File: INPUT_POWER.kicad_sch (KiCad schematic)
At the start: 30 parts, among them J1 TYPE-C-31-M12_13, SW3 ON/OFF, U3 IP5306

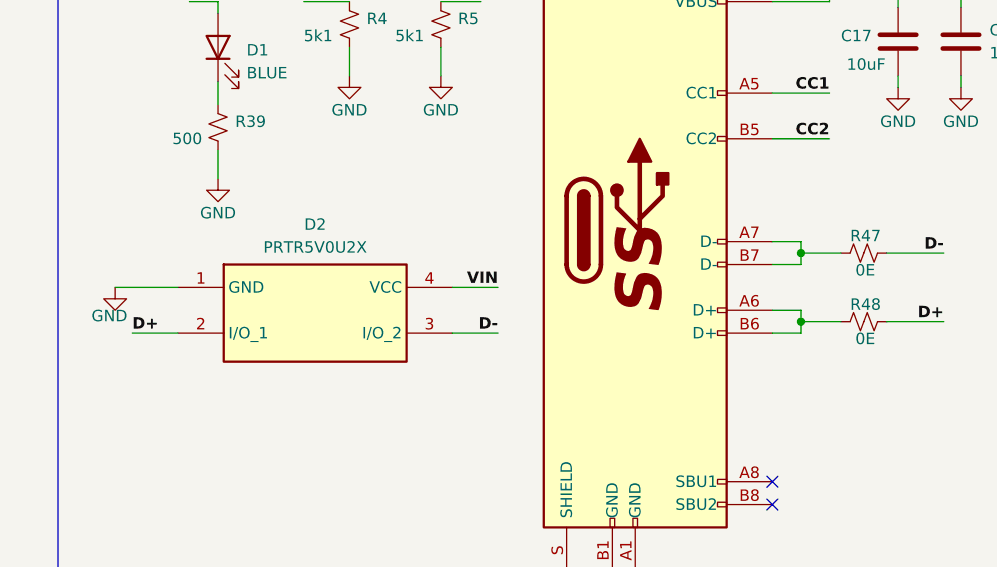
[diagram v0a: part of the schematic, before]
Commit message: Completed routing for USB peripheral for CH340
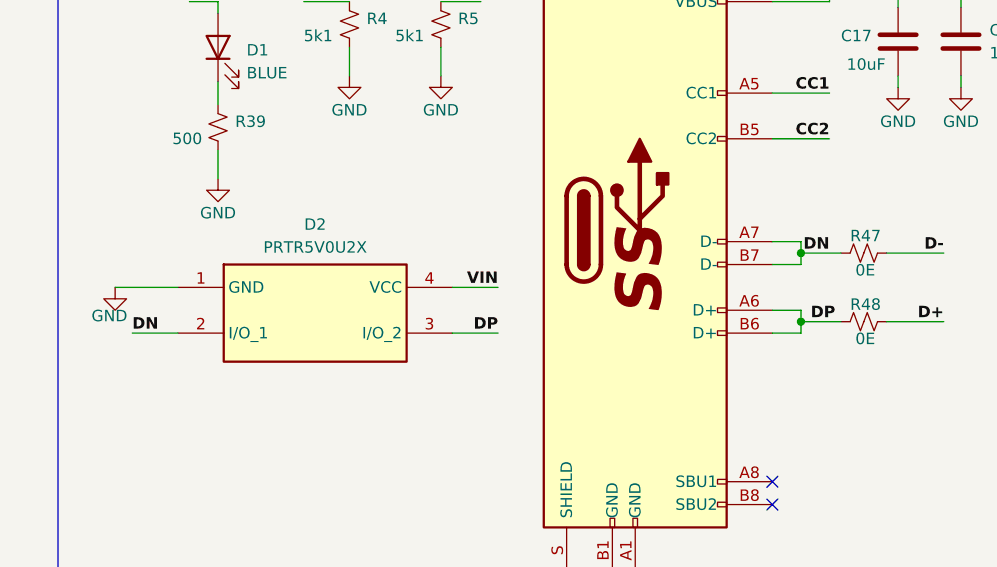
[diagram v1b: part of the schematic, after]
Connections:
- net D+: no longer D2.2 (I/O_1)
- net D-: no longer D2.3 (I/O_2)
- net DP: now reaches J1.A6 (D+), J1.B6 (D+), R48.1
- net DP: now also D2.3 (I/O_2)
- net DN: now reaches J1.A7 (D-), J1.B7 (D-), R47.1
- net DN: now also D2.2 (I/O_1)
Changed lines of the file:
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@@
     (effects (font (size 1.27 1.27) bold (color 0 255 0 1)) (justify left bottom))
   )
-  (label "D-" (at 69.215 95.25 180) (fields_autoplaced)
-    (effects (font (size 1.27 1.27) (thickness 0.254) bold (color 0 0 255 1)) (justify right bottom))
+  (label "DN" (at 28.575 95.25 0) (fields_autoplaced)
+    (effects (font (size 1.27 1.27) (thickness 0.254) bold (color 0 0 255 1)) (justify left bottom))
   )
   (label "V_BAT" (at 38.735 185.42 180) (fields_autoplaced)
@@
     (effects (font (size 1.27 1.27) bold (color 255 0 0 1)) (justify left bottom))
   )
+  (label "DP" (at 106.68 93.98 180) (fields_autoplaced)
+    (effects (font (size 1.27 1.27) (thickness 0.254) bold (color 0 0 255 1)) (justify right bottom))
+  )
   (label "VIN" (at 69.215 90.17 180) (fields_autoplaced)
     (effects (font (size 1.27 1.27) (thickness 0.254) bold (color 255 0 0 1)) (justify right bottom))
@@
     (effects (font (size 1.27 1.27) (thickness 0.254) bold (color 255 0 0 1)) (justify left bottom))
   )
-  (label "D+" (at 28.575 95.25 0) (fields_autoplaced)
-    (effects (font (size 1.27 1.27) (thickness 0.254) bold (color 0 0 255 1)) (justify left bottom))
+  (label "DP" (at 69.215 95.25 180) (fields_autoplaced)
+    (effects (font (size 1.27 1.27) (thickness 0.254) bold (color 0 0 255 1)) (justify right bottom))
   )
   (label "VOUT" (at 274.955 73.025 180) (fields_autoplaced)
@@
     (effects (font (size 1.27 1.27) bold (color 0 255 0 1)) (justify left bottom))
   )
+  (label "DN" (at 106.045 86.36 180) (fields_autoplaced)
+    (effects (font (size 1.27 1.27) (thickness 0.254) bold (color 0 0 255 1)) (justify right bottom))
+  )
   (label "CC2" (at 67.31 58.42 180) (fields_autoplaced)

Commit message: Merge changes upstream
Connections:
- net D+: now also D2.2 (I/O_1)
- net D-: now also D2.3 (I/O_2)
- net DN: no longer names the net of J1.A7 (D-), J1.B7 (D-), R47.1
- net DN: no longer D2.2 (I/O_1)
- net DP: no longer names the net of J1.A6 (D+), J1.B6 (D+), R48.1
- net DP: no longer D2.3 (I/O_2)
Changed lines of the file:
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@@
     (effects (font (size 1.27 1.27) bold (color 0 255 0 1)) (justify left bottom))
   )
-  (label "DN" (at 28.575 95.25 0) (fields_autoplaced)
-    (effects (font (size 1.27 1.27) (thickness 0.254) bold (color 0 0 255 1)) (justify left bottom))
+  (label "D-" (at 69.215 95.25 180) (fields_autoplaced)
+    (effects (font (size 1.27 1.27) (thickness 0.254) bold (color 0 0 255 1)) (justify right bottom))
   )
   (label "V_BAT" (at 38.735 185.42 180) (fields_autoplaced)
@@
     (effects (font (size 1.27 1.27) bold (color 255 0 0 1)) (justify left bottom))
   )
-  (label "DP" (at 106.68 93.98 180) (fields_autoplaced)
-    (effects (font (size 1.27 1.27) (thickness 0.254) bold (color 0 0 255 1)) (justify right bottom))
-  )
   (label "VIN" (at 69.215 90.17 180) (fields_autoplaced)
     (effects (font (size 1.27 1.27) (thickness 0.254) bold (color 255 0 0 1)) (justify right bottom))
@@
     (effects (font (size 1.27 1.27) (thickness 0.254) bold (color 255 0 0 1)) (justify left bottom))
   )
-  (label "DP" (at 69.215 95.25 180) (fields_autoplaced)
-    (effects (font (size 1.27 1.27) (thickness 0.254) bold (color 0 0 255 1)) (justify right bottom))
+  (label "D+" (at 28.575 95.25 0) (fields_autoplaced)
+    (effects (font (size 1.27 1.27) (thickness 0.254) bold (color 0 0 255 1)) (justify left bottom))
   )
   (label "VOUT" (at 274.955 73.025 180) (fields_autoplaced)
@@
     (effects (font (size 1.27 1.27) bold (color 0 255 0 1)) (justify left bottom))
   )
-  (label "DN" (at 106.045 86.36 180) (fields_autoplaced)
-    (effects (font (size 1.27 1.27) (thickness 0.254) bold (color 0 0 255 1)) (justify right bottom))
-  )
   (label "CC2" (at 67.31 58.42 180) (fields_autoplaced)
